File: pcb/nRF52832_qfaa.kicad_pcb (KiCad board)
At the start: 4 copper layers, 24.4 x 36.5 mm, 39 parts, among them J1 Battery, J2 Conn_02x05_Odd_Even, J3 Conn_01x03_Male, U1 NRF52832, U2 LED-Button, U3 TLV75533PDBVR, U4 SPU0410HR5H, U5 W25Q32JVZP, X1 32MHz, X2 32.768kHz

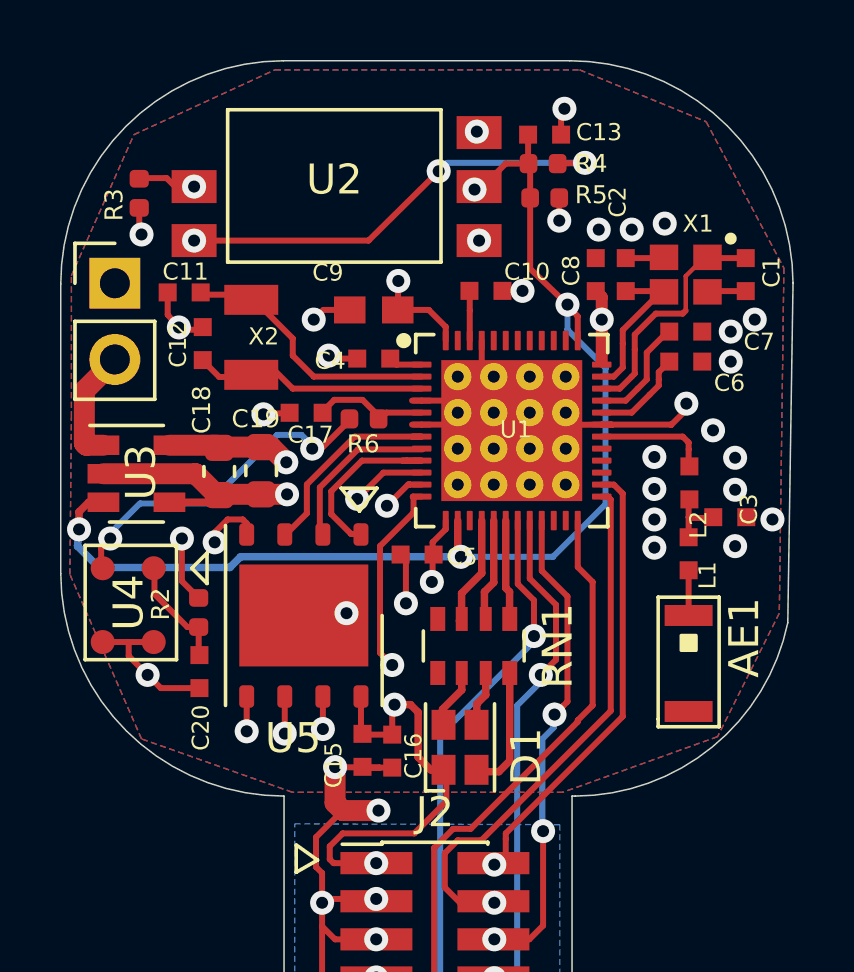
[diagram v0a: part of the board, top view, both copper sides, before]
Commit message: [pcb] added electrical OR for multiple power inputs
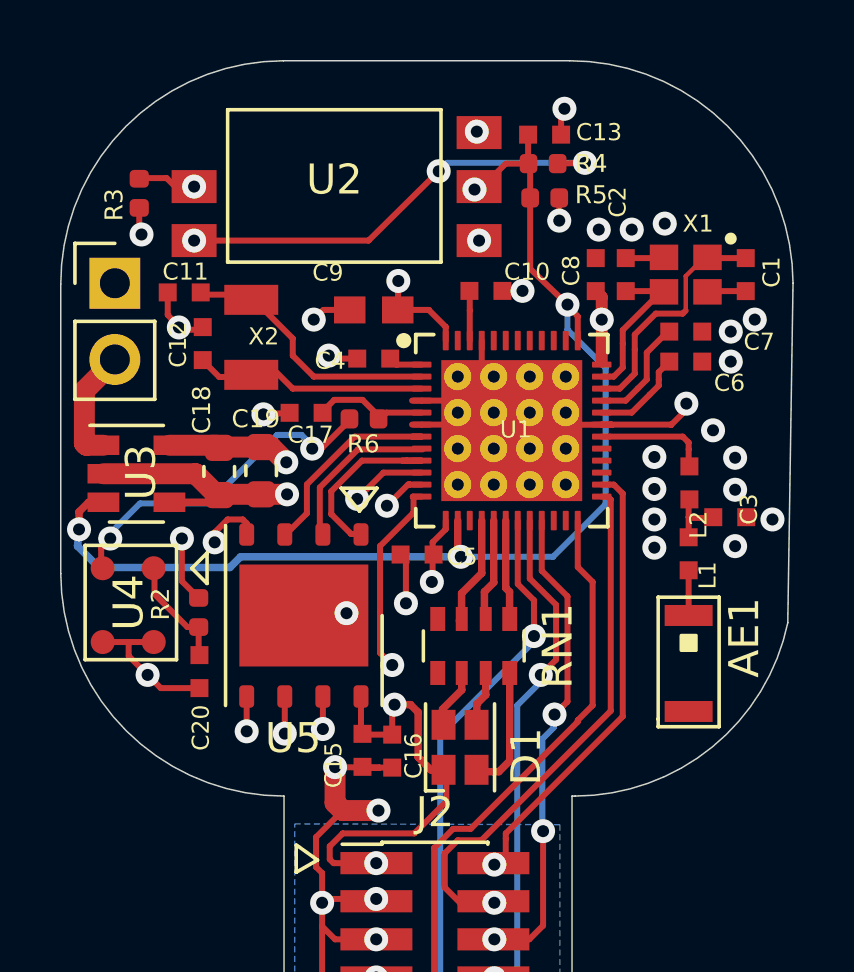
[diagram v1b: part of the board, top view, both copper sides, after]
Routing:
- removed copper zone on F.Cu, net GND
- removed copper zone on In1.Cu, net GND
- removed copper zone on In2.Cu, net VCC

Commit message: hw version 1.1 draft
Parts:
- removed AE1: Antenna_Chip, voice_recorder:ANT_2450AT18B100
- removed the C17 at (142.6, 105.4)
- removed the C18 at (139.8, 107.4)
- removed J1: Battery, Connector_PinHeader_2.54mm:PinHeader_1x02_P2.54mm_Vertical
- removed J3: Conn_01x03_Male, Connector_PinHeader_2.54mm:PinHeader_1x03_P2.54mm_Vertical
- removed the L2 at (155.4, 107.7)
- removed U5: W25Q32JVZP, Package_SON:WSON-8-1EP_6x5mm_P1.27mm_EP3.4x4.3mm
- added C1: 10uF, Capacitor_SMD:C_0402_1005Metric, F.Cu at (133.0, 80.8)
- added C2: 10uF, Capacitor_SMD:C_0402_1005Metric, F.Cu at (118.7, 80.3)
- added C20: 4.7uF, Capacitor_SMD:C_0402_1005Metric, F.Cu at (131.2, 71.1)
- added C21: 4.7uF, Capacitor_SMD:C_0402_1005Metric, F.Cu at (138.3, 79.5)
- added C22: 0.8pF, Capacitor_SMD:C_0402_1005Metric, F.Cu at (112.3, 72.8)
- added D2: BAS40-05,215, Package_TO_SOT_SMD:SOT-23, F.Cu at (130.7, 79.9)
- added D3: LED, LED_SMD:LED_0603_1608Metric, F.Cu at (132.6, 76.2)
- added H1: MountingHole, nRF52832_qfaa:MountingHole_1mm, F.Cu at (136.0, 76.0)
- added H2: MountingHole, nRF52832_qfaa:MountingHole_1mm, F.Cu at (100.0, 76.0)
- added JP1: Jumper_2_Open, Jumper:SolderJumper-2_P1.3mm_Open_RoundedPad1.0x1.5mm, B.Cu at (130.9, 79.9)
- added MK1: SPM1423HM4H, Sensor_Audio:ST_HLGA-6_3.76x4.72mm_P1.65mm, F.Cu at (105.2, 79.0)
- added R10: 100K, Resistor_SMD:R_0402_1005Metric, F.Cu at (131.2, 73.0)
- added R11: 100K, Resistor_SMD:R_0402_1005Metric, F.Cu at (131.2, 75.1)
- added R5: 1.6K, Resistor_SMD:R_0402_1005Metric, F.Cu at (127.9, 80.3)
- added R7: 10K, Resistor_SMD:R_0402_1005Metric, F.Cu at (137.5, 71.8)
- added R8: 1.18K, Resistor_SMD:R_0402_1005Metric, F.Cu at (138.3, 75.3)
- added R9: 1K, Resistor_SMD:R_0402_1005Metric, F.Cu at (133.9, 76.1)
- added S1: KMR221GLFS, _other:SW_KMR221GLFS, F.Cu at (108.0, 73.8)
- added TP1: b+, TestPoint:TestPoint_Pad_D1.0mm, B.Cu at (131.0, 72.0)
- added TP2: chg, TestPoint:TestPoint_Pad_D1.0mm, B.Cu at (138.0, 77.8)
- added TP3: b-, TestPoint:TestPoint_Pad_D1.0mm, B.Cu at (131.0, 75.0)
- added TP4: gnd, TestPoint:TestPoint_Pad_D1.0mm, B.Cu at (138.0, 74.2)
- added TP5: Antenna, TestPoint:TestPoint_Pad_D1.0mm, F.Cu at (113.8, 71.1)
- added TP6: TestPoint, TestPoint:TestPoint_Pad_D1.0mm, B.Cu at (119.3, 71.1)
- added TP7: TestPoint, TestPoint:TestPoint_Pad_D1.0mm, B.Cu at (121.3, 71.1)
- added TP8: TestPoint, TestPoint:TestPoint_Pad_D1.0mm, B.Cu at (122.8, 72.6)
- C10: renamed from C2; value 12pF -> 10pF; footprint nRF52832_qfaa:RESC0402_N -> Capacitor_SMD:C_0402_1005Metric
- C11, C12: value 12pF -> 10pF; footprint nRF52832_qfaa:RESC0402_N -> Capacitor_SMD:C_0402_1005Metric
- C13: renamed from C1; value 12pF -> 10pF; footprint nRF52832_qfaa:RESC0402_N -> Capacitor_SMD:C_0402_1005Metric
- C14: renamed from C3; value 1.2pF -> 0.8pF; footprint nRF52832_qfaa:RESC0402_N -> Capacitor_SMD:C_0402_1005Metric
- C15: renamed from C20; footprint nRF52832_qfaa:RESC0402_N -> Capacitor_SMD:C_0402_1005Metric
- C16: renamed from C5; footprint nRF52832_qfaa:RESC0402_N -> Capacitor_SMD:C_0402_1005Metric
- C17: renamed from C15; footprint nRF52832_qfaa:RESC0402_N -> Capacitor_SMD:C_0402_1005Metric
- C18: renamed from C16; footprint nRF52832_qfaa:RESC0402_N -> Capacitor_SMD:C_0402_1005Metric
- C19: value 10uF -> 1uF; footprint Capacitor_SMD:C_0603_1608Metric -> Capacitor_SMD:C_0402_1005Metric
- C3: renamed from C13; footprint nRF52832_qfaa:RESC0402_N -> Capacitor_SMD:C_0402_1005Metric
- C4: renamed from C10; footprint nRF52832_qfaa:RESC0402_N -> Capacitor_SMD:C_0402_1005Metric
- C5: renamed from C9; footprint nRF52832_qfaa:RESC0603_N -> Capacitor_SMD:C_0402_1005Metric
- C6: renamed from C8; footprint nRF52832_qfaa:RESC0402_N -> Capacitor_SMD:C_0402_1005Metric
- C7: footprint nRF52832_qfaa:RESC0402_N -> Capacitor_SMD:C_0402_1005Metric
- C8: renamed from C6; footprint nRF52832_qfaa:RESC0402_N -> Capacitor_SMD:C_0402_1005Metric
- C9: renamed from C4; footprint nRF52832_qfaa:RESC0402_N -> Capacitor_SMD:C_0402_1005Metric
- D1: footprint LED_SMD:LED_Cree-PLCC4_2x2mm_CW -> nRF52832_qfaa:LED_Cree-PLCC4_2x2mm_CW
- J2: moved to B.Cu
- L2: renamed from L1; footprint nRF52832_qfaa:RESC0402_N -> Capacitor_SMD:C_0402_1005Metric
- R1: renamed from R5; value 1M -> 100K
- R2: value 330 -> 100K
- R4: value 330 -> 10K
- R6: value 330 -> 1.13K
- RN1: footprint Resistor_SMD:R_Array_Convex_4x0603 -> Resistor_SMD:R_Array_Convex_4x0402
- U2: value LED-Button -> W25Q32JVZP; footprint voice_recorder:LED_BUTTON -> nRF52832_qfaa:WSON-8-1EP_6x5mm_P1.27mm_EP3.4x4.3mm
- U4: value SPU0410HR5H -> BQ24078RGTR; footprint voice_recorder:SPU0410HR5H -> _other:VQFN-16-1EP_3x3mm_P0.5mm_EP1.45x1.45mm_ThermalVias
- moved J2 64.0 mm to (105.1, 74.5)
- moved D1 61.0 mm to (103.3, 74.9)
- moved RN1 60.9 mm to (103.4, 72.0)
- moved L2 55.5 mm to (113.8, 73.3), turned to 90 degrees
- moved C14 55.2 mm to (113.4, 74.8), turned to 0 degrees
- moved C15 52.1 mm to (101.5, 78.0), turned to 180 degrees
- moved C8 51.5 mm to (111.9, 75.9), turned to 180 degrees
- moved C7 50.4 mm to (111.9, 77.0), turned to 180 degrees
- moved C13 49.9 mm to (112.1, 79.5)
- moved X2 46.8 mm to (113.9, 79.2), turned to 270 degrees
- moved C16 45.3 mm to (122.4, 71.6), turned to 90 degrees
- moved C10 44.3 mm to (113.6, 81.2), turned to 180 degrees
- moved U1 43.3 mm to (118.9, 75.3), turned to 180 degrees
- moved C6 42.4 mm to (115.8, 79.2), turned to 270 degrees
- moved C18 42.3 mm to (129.8, 77.5), turned to 180 degrees
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- renumbered X2 to X1, X1 to X2
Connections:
- C14 pad 2: Net-(C3-Pad2) -> Net-(C14-Pad2)
- C15 pad 1: Net-(C20-Pad1) -> Net-(C15-Pad1)
- C19 pad 1: VCC -> GND
- C19 pad 2: GND -> V_charger
- C3 pad 1: /BUTTON -> MAIN_BUTTON
- C9 pad 1: /DEC1 -> GND
- C9 pad 2: GND -> /DEC1
- J2 pad 7: Net-(J2-Pad7) -> (no net)
- J2 pad 8: Net-(J2-Pad8) -> (no net)
- L2 pad 1: Net-(C3-Pad2) -> Net-(C14-Pad2)
- R1 pad 1: /BUTTON -> MAIN_BUTTON
- R2 pad 1: Net-(C20-Pad1) -> DBG_POWER_LATCH
- R2 pad 2: VCC -> GND
- R3 pad 1: Net-(R3-Pad1) -> Net-(C15-Pad1)
- R3 pad 2: GND -> VCC
- R4 pad 1: /BUTTON -> /Power/LDO_EN
- R4 pad 2: Net-(R4-Pad2) -> VCC
- R6 pad 1: /MIC_OUT -> GND
- R6 pad 2: /P0.02 -> Net-(R6-Pad2)
- RN1 pad 4: Net-(RN1-Pad4) -> (no net)
- RN1 pad 5: Net-(RN1-Pad5) -> (no net)
- U1 pad 10: /MEM_DI -> /MEM_CS
- U1 pad 11: /MEM_CLK -> /MEM_DO
- U1 pad 12: /MEM_IO3 -> /MEM_IO2
- U1 pad 14: /BUTTON -> /P0.11
- U1 pad 15: Net-(U1-Pad15) -> /P0.12
- U1 pad 19: /P0.16 -> (no net)
- U1 pad 20: /P0.17 -> (no net)
- U1 pad 22: /P0.19 -> (no net)
- U1 pad 23: /P0.20 -> (no net)
- U1 pad 27: /P0.22 -> (no net)
- U1 pad 28: /P0.23 -> (no net)
- U1 pad 29: /P0.24 -> (no net)
- U1 pad 30: Net-(L2-Pad2) -> Net-(C14-Pad2)
- U1 pad 37: /BUTTON -> MAIN_BUTTON
- U1 pad 38: /P0.26 -> DBG_POWER_LATCH
- U1 pad 39: /P0.27 -> MCU_POWER_LATCH
- U1 pad 41: Net-(U1-Pad41) -> /P0.29
- U1 pad 42: Net-(U1-Pad42) -> (no net)
- U1 pad 43: Net-(U1-Pad43) -> (no net)
- U1 pad 44: Net-(U1-Pad44) -> (no net)
- U1 pad 47: Net-(U1-Pad47) -> (no net)
- U1 pad 5: /P0.02 -> VBAT_LEVEL
- U1 pad 7: /MEM_IO2 -> /MEM_DI
- U1 pad 8: /MEM_DO -> /MEM_IO3
- U1 pad 9: /MEM_CS -> /MEM_CLK
- U2 pad 1: +BATT -> /MEM_CS
- U2 pad 2: /BUTTON -> /MEM_DO
- U2 pad 3: +BATT -> /MEM_IO2
- U2 pad 4: Net-(R4-Pad2) -> GND
- U2 pad 5: Net-(R3-Pad1) -> /MEM_DI
- U3 pad 1: +BATT -> VSS
- U3 pad 3: /BUTTON -> /Power/LDO_EN
- U4 pad 1: Net-(C20-Pad1) -> Net-(R7-Pad2)
- U4 pad 2: GND -> +BATT
- U4 pad 3: GND -> +BATT
- U4 pad 4: /MIC_OUT -> GND
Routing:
- net VSS: track 0.00 -> 54.5 mm, vias 0 -> 3
- net VCC: track 28.6 -> 80.9 mm, vias 7 -> 10
- net GND: track 78.8 -> 122.0 mm, vias 35 -> 45
- net /BUTTON: track 38.4 -> 0.00 mm, vias 4 -> 0
- net MAIN_BUTTON: track 0.00 -> 35.7 mm, vias 0 -> 3
- net DBG_POWER_LATCH: track 0.00 -> 21.3 mm, vias 0 -> 2
- net /P0.16: track 21.1 -> 0.00 mm, vias 1 -> 0
- net +BATT: track 26.8 -> 5.68 mm
- net /P0.17: track 20.0 -> 0.00 mm, vias 1 -> 0
- net /P0.29: track 0.00 -> 16.5 mm, vias 0 -> 2
- net /LED_RED: track 3.65 -> 18.9 mm, vias 0 -> 2
- net Net-(R4-Pad2): track 15.1 -> 0.00 mm, vias 3 -> 0
- net /LED_BLUE: track 3.55 -> 17.4 mm, vias 0 -> 2
- net V_charger: track 0.00 -> 13.4 mm, vias 0 -> 3
- net /P0.28: track 0.00 -> 13.4 mm, vias 0 -> 2
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- added copper zone on F.Cu, net GND
- added copper zone on In1.Cu, net GND
- added copper zone on In2.Cu, net VCC
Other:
- board size 24.4 x 36.5 mm -> 41 x 12 mm
- rule trace_min: 0.15 -> 0.12
- rule via_min_drill: 0.3 -> 0.2
- rule via_min_size: 0.4 -> 0.45
- board text added: "Dictofun 1.1"
- board text added: "ant"
- board text added: "dbg on"
- board text added: "github.com/rundb/dictofun"
- board text added: "gnd"
- board text added: "rx"
- board text added: "tx"
- board text removed: "+"
- board text removed: "-"
- board text removed: "GND"
- board text removed: "RX"
- board text removed: "TX"
- board text removed: "dictofun 1.0"

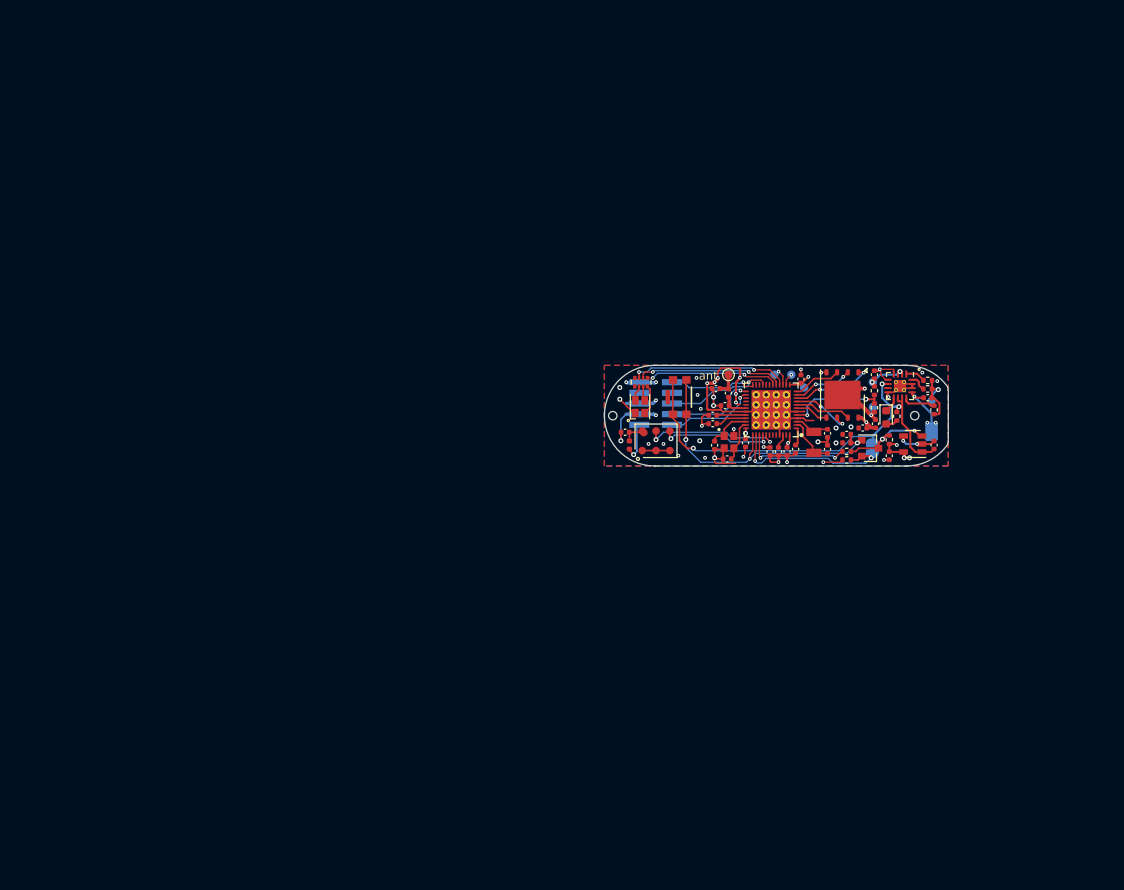
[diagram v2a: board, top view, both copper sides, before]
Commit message: [pcb] added fabrication outputs for the jlcpcb order
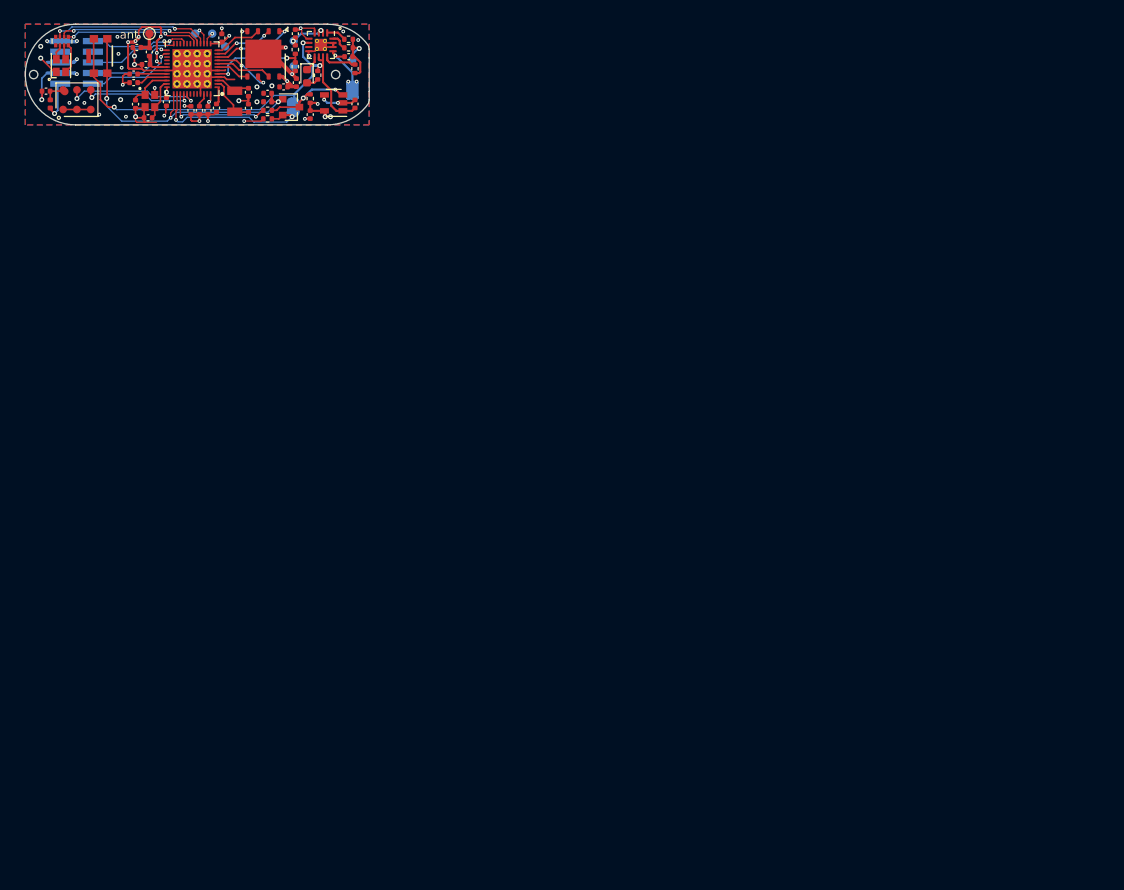
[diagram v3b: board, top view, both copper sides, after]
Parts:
- C22: value 0.8pF -> DNP
- D1: value ASMB-MTB0-0A3A2 -> ASMB-LTC2-0A335
- moved C17 80.1 mm to (62.3, 36.3)
- moved C20 80.1 mm to (62.2, 30.5)
- moved C7 80.1 mm to (42.9, 36.3)
- moved D1 80.1 mm to (34.2, 34.3)
- moved J2 80.1 mm to (36.1, 33.9)
- moved R11 80.1 mm to (62.2, 34.4)
- moved U1 80.1 mm to (49.9, 34.6)
- moved C10 80.1 mm to (44.6, 40.5)
- moved C13 80.1 mm to (43.1, 38.9)
- moved C14 80.1 mm to (44.3, 34.1)
- moved C15 80.1 mm to (32.4, 37.3)
- moved C16 80.1 mm to (53.4, 31.0)
- moved C18 80.1 mm to (60.8, 36.8)
- moved C19 80.1 mm to (68.5, 33.2)
- moved C2 80.1 mm to (49.7, 39.6)
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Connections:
- J2 pad 7: (no net) -> Net-(J2-Pad7)
- J2 pad 8: (no net) -> Net-(J2-Pad8)
- RN1 pad 4: (no net) -> Net-(RN1-Pad4)
- RN1 pad 5: (no net) -> Net-(RN1-Pad5)
- U1 pad 19: (no net) -> /P0.16
- U1 pad 20: (no net) -> /P0.17
- U1 pad 22: (no net) -> /P0.19
- U1 pad 23: (no net) -> /P0.20
- U1 pad 27: (no net) -> /P0.22
- U1 pad 28: (no net) -> /P0.23
- U1 pad 29: (no net) -> /P0.24
- U1 pad 42: (no net) -> Net-(U1-Pad42)
- U1 pad 43: (no net) -> Net-(U1-Pad43)
- U1 pad 44: (no net) -> Net-(U1-Pad44)
- U1 pad 47: (no net) -> Net-(U1-Pad47)
- U4 pad 7: (no net) -> Net-(U4-Pad7)
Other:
- rule pad_to_mask_clearance: 0.051 -> 0

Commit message: [pcb] v1.2 schematics and PCB, start of the fixture
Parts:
- removed JP1: Jumper_2_Open, Jumper:SolderJumper-2_P1.3mm_Open_RoundedPad1.0x1.5mm
- removed R2: 100K, Resistor_SMD:R_0402_1005Metric
- removed R4: 10K, Resistor_SMD:R_0402_1005Metric
- removed TP5: Antenna, TestPoint:TestPoint_Pad_D1.0mm
- added C23: 100pF, Capacitor_SMD:C_0402_1005Metric, F.Cu at (64.1, 37.9)
- added J1: Conn_01x01_Female, Connector_PinHeader_1.00mm:PinHeader_1x01_P1.00mm_Vertical, F.Cu at (40.5, 30.2)
- added R13: 330, Resistor_SMD:R_0402_1005Metric, F.Cu at (43.2, 38.9)
- added TP10: TestPoint, TestPoint:TestPoint_Pad_D1.0mm, B.Cu at (35.8, 40.8)
- added TP11: TestPoint, TestPoint:TestPoint_Pad_D1.0mm, B.Cu at (43.8, 41.1)
- added TP12: TestPoint, TestPoint:TestPoint_Pad_D1.0mm, B.Cu at (56.1, 36.2)
- added TP13: TestPoint, TestPoint:TestPoint_Pad_D1.0mm, B.Cu at (57.1, 30.0)
- added TP14: TestPoint, TestPoint:TestPoint_Pad_D1.0mm, B.Cu at (59.6, 30.0)
- added TP15: TestPoint, TestPoint:TestPoint_Pad_D1.0mm, B.Cu at (54.5, 32.8)
- added TP16: TestPoint, TestPoint:TestPoint_Pad_D1.0mm, B.Cu at (59.1, 40.8)
- added TP17: TestPoint, TestPoint:TestPoint_Pad_D1.0mm, B.Cu at (54.0, 38.7)
- added TP18: TestPoint, TestPoint:TestPoint_Pad_D1.0mm, B.Cu at (53.1, 30.0)
- added TP19: TestPoint, TestPoint:TestPoint_Pad_D1.0mm, B.Cu at (55.0, 40.9)
- added TP20: TestPoint, TestPoint:TestPoint_Pad_D1.0mm, F.Cu at (50.3, 30.1)
- added TP21: TestPoint, TestPoint:TestPoint_Pad_D1.0mm, F.Cu at (55.0, 30.5)
- added TP22: TestPoint, TestPoint:TestPoint_Pad_D1.0mm, F.Cu at (51.7, 30.9)
- added TP23: TestPoint, TestPoint:TestPoint_Pad_D1.0mm, F.Cu at (53.3, 30.2)
- added TP24: TestPoint, TestPoint:TestPoint_Pad_D1.0mm, F.Cu at (55.1, 37.3)
- added TP25: TestPoint, TestPoint:TestPoint_Pad_D1.0mm, F.Cu at (55.6, 39.0)
- added TP26: TestPoint, TestPoint:TestPoint_Pad_D1.0mm, F.Cu at (69.5, 36.7)
- added TP27: TestPoint, TestPoint:TestPoint_Pad_D1.0mm, F.Cu at (53.8, 40.1)
- added TP28: TestPoint, TestPoint:TestPoint_Pad_D1.0mm, F.Cu at (55.9, 40.8)
- added TP9: TestPoint, TestPoint:TestPoint_Pad_D1.0mm, B.Cu at (38.0, 40.8)
- moved S1 13.7 mm to (52.6, 34.9), turned to -90 degrees
- moved C11 6.60 mm to (50.1, 40.8), turned to 180 degrees
- moved C12 5.63 mm to (52.0, 40.8), turned to 0 degrees
- moved C6 4.64 mm to (42.1, 38.6)
- moved X2 4.58 mm to (40.2, 38.5)
- moved C13 4.38 mm to (38.7, 38.9)
- moved C2 4.20 mm to (45.5, 39.9)
- moved C10 4.19 mm to (40.4, 40.5)
- moved C16 4.19 mm to (49.2, 31.0)
- moved C22 4.19 mm to (39.1, 32.1)
- moved C5 4.19 mm to (47.5, 39.6)
- moved C9 4.19 mm to (48.6, 39.3)
- moved L2 4.19 mm to (40.6, 32.6)
- moved U1 4.19 mm to (45.7, 34.6)
- moved C14 4.19 mm to (40.2, 34.1)
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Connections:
- net /P0.00/XL1 renamed /P0.00/XL1
- net /P0.01/XL2 renamed /P0.01/XL2
- net /P0.18/SWO renamed /P0.18/SWO
- net /P0.21/RESET renamed /P0.21/RESET
- D2 pad 2: DBG_POWER_LATCH -> unconnected-(D2-Pad2)
- J2 pad 7: Net-(J2-Pad7) -> unconnected-(J2-Pad7)
- J2 pad 8: Net-(J2-Pad8) -> unconnected-(J2-Pad8)
- RN1 pad 4: Net-(RN1-Pad4) -> unconnected-(RN1-Pad4)
- RN1 pad 5: Net-(RN1-Pad5) -> unconnected-(RN1-Pad5)
- U1 pad 37: MAIN_BUTTON -> /P0.25
- U1 pad 38: DBG_POWER_LATCH -> unconnected-(U1-Pad38)
- U1 pad 42: Net-(U1-Pad42) -> unconnected-(U1-Pad42)
- U1 pad 43: Net-(U1-Pad43) -> unconnected-(U1-Pad43)
- U1 pad 44: Net-(U1-Pad44) -> unconnected-(U1-Pad44)
- U1 pad 47: Net-(U1-Pad47) -> unconnected-(U1-Pad47)
- U4 pad 7: Net-(U4-Pad7) -> unconnected-(U4-Pad7)
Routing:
- net +BATT: track 5.68 -> 30.8 mm, vias 2 -> 3
- net DBG_POWER_LATCH: track 21.3 -> 0.00 mm, vias 2 -> 0
- net VSS: track 54.5 -> 39.9 mm, vias 3 -> 4
- net /MEM_CS: track 9.94 -> 19.9 mm
- net /SWDCLK: track 11.0 -> 20.9 mm, vias 1 -> 3
- net /SWDIO: track 10.7 -> 20.5 mm, vias 1 -> 3
- net MAIN_BUTTON: track 35.7 -> 27.1 mm, vias 3 -> 4
- net /LED_RED: track 18.9 -> 11.9 mm
- net /MEM_DO: track 7.25 -> 14.1 mm, vias 2 -> 3
- net VCC: track 80.9 -> 86.9 mm, vias 10 -> 12
- net /LED_BLUE: track 17.4 -> 11.6 mm
- net /MEM_DI: track 4.05 -> 9.58 mm, vias 0 -> 1
- net /MEM_CLK: track 7.66 -> 13.0 mm
- net /DEC4: track 1.69 -> 6.90 mm, vias 0 -> 1
- net /MEM_IO3: track 6.76 -> 11.4 mm
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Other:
- board size 41 x 12 mm -> 41.5 x 13 mm
- net class Default removed
- board text added: "Dictofun 1.2"
- board text removed: "Dictofun 1.1"
- board text removed: "dbg on"
